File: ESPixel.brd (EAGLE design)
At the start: 35.1 x 46 mm, 15 parts, among them Q1 MOSFET-NCHANNEL2N7000

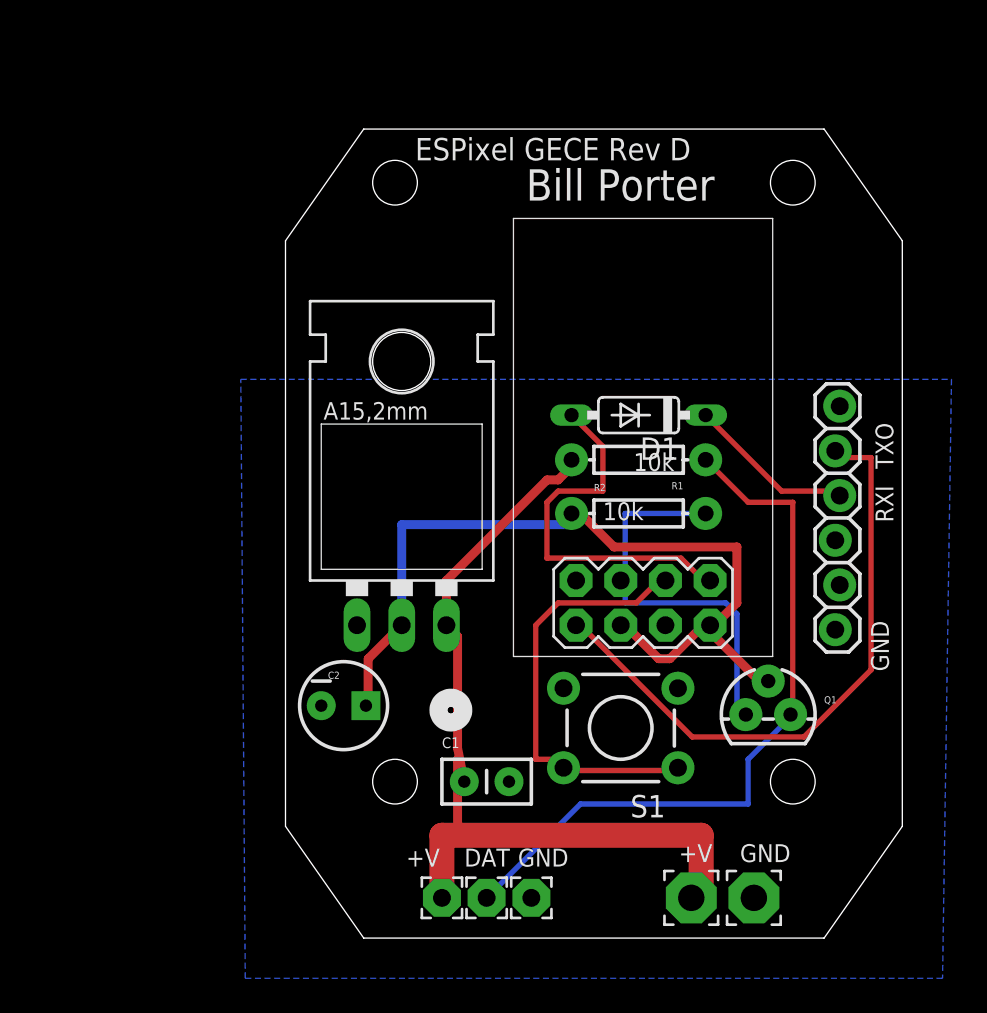
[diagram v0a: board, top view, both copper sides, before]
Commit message: Added Diode to GECE and added WS2811 version
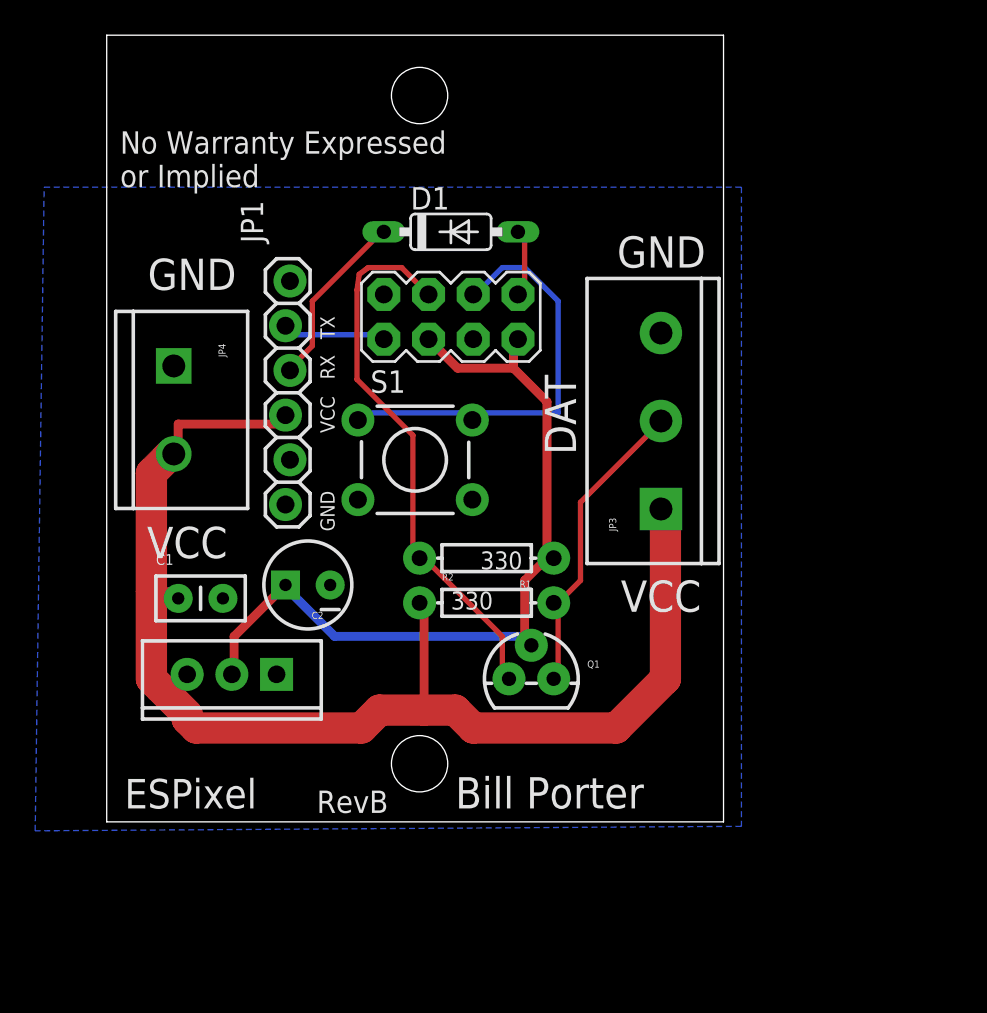
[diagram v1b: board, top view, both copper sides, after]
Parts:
- removed PAD1, PAD2: 2.9/1.5, wirepad:2.9/1.5
- removed PAD3, PAD4, PAD5: (no value), wirepad:2,15/1,0
- added JP3: (no value), SparkFun-Connectors:SCREWTERMINAL-5MM-3
- added JP4: M025MM, SparkFun-Connectors:SCREWTERMINAL-5MM-2
- C1: value .1u -> (none)
- C2: value 10u -> (none)
- R1, R2: value 10k -> 330
- U$3: value V_REG_LD1117VXX -> V_REG_317SINK; device SparkFun-PowerIC:78XXL -> SparkFun-PowerIC:TO220-ADJ
- moved JP1 32.0 mm to (21.6, 46.2)
- moved U$2 19.6 mm to (30.7, 44.2)
- moved C1 19.3 mm to (15.2, 28.2)
- moved S1 19.2 mm to (28.7, 36.1), turned to 0 degrees
- moved D1 14.9 mm to (30.7, 49.0), turned to 0 degrees
- moved Q1 13.6 mm to (35.3, 23.6)
- moved U$3 11.7 mm to (18.3, 23.9), turned to 180 degrees
- moved R1 10.3 mm to (32.8, 30.5)
- moved R2 10.0 mm to (32.8, 27.9)
- moved C2 7.15 mm to (22.6, 29.0), turned to 180 degrees
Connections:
- net 3.3V: now also R1.P$1, U$3.OUT; no longer R2.P$1, U$3.GND
- net 5V: now also JP1.4, JP3.1, JP4.2, R2.P$1, U$3.IN; no longer PAD2.1, PAD5.1, R1.P$2, U$3.OUT
- net GND: now also JP3.3, JP4.1, U$3.ADJ; no longer PAD1.1, PAD3.1, U$3.IN
- net N$4: now also JP3.2, R2.P$2; no longer PAD4.1, R1.P$1
- net N$6: now also R1.P$2; no longer R2.P$2
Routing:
- net N$1: track 35.3 -> 6.01 mm
- net N$4: track 41.6 -> 17.4 mm
- net 5V: track 50.9 -> 74.3 mm
- net N$9: track 21.5 -> 4.03 mm
- net N$6: track 22.7 -> 31.6 mm
- net 3.3V: track 49.1 -> 46.6 mm
- net N$8: track 9.57 -> 10.1 mm
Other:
- board size 35.1 x 46 mm -> 35.1 x 44.7 mm
- board text added: "ESPixel"
- board text added: "RX"
- board text added: "RevB"
- board text added: "TX"
- board text added: "VCC"
- board text removed: "+V"
- board text removed: "ESPixel GECE Rev D"
- board text removed: "RXI"
- board text removed: "TXO"
